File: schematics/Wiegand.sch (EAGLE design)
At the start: 66 parts, among them IC1 MC33269ST-3.3T3, J1 AVR_SPI_PRG_6NS, Q1 NTR1P02T1G, Q2 NTR1P02T1G, U1 ATMEGA168, U2 RS485_SP491, U4 MOC3063, U5 MOC3063, U6 MOC3063, U7 MOC3063, U8 MOC3063, U9 MOC3063, Y1 16Mhz

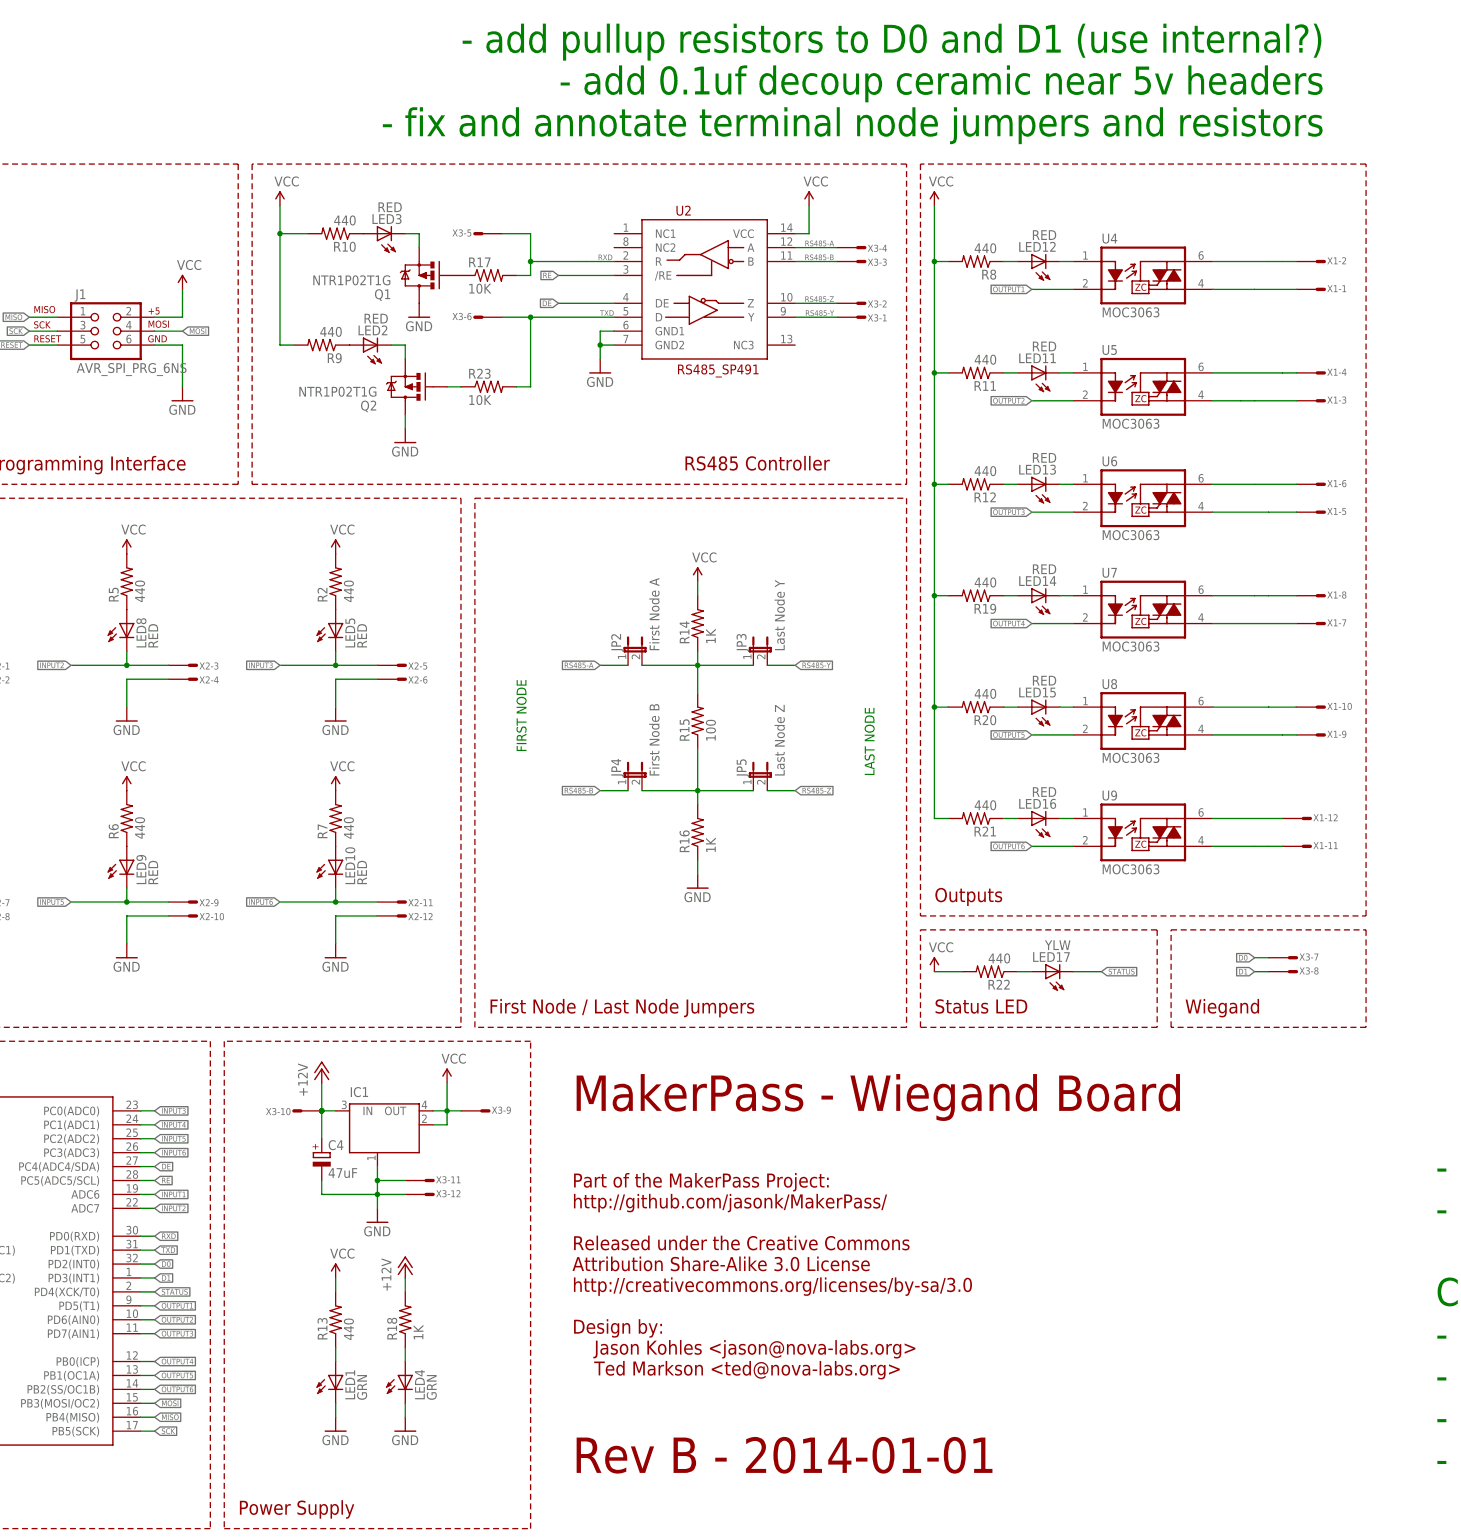
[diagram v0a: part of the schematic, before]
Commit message: added separate resistors for first / last node, added transistor option atop optoisolators
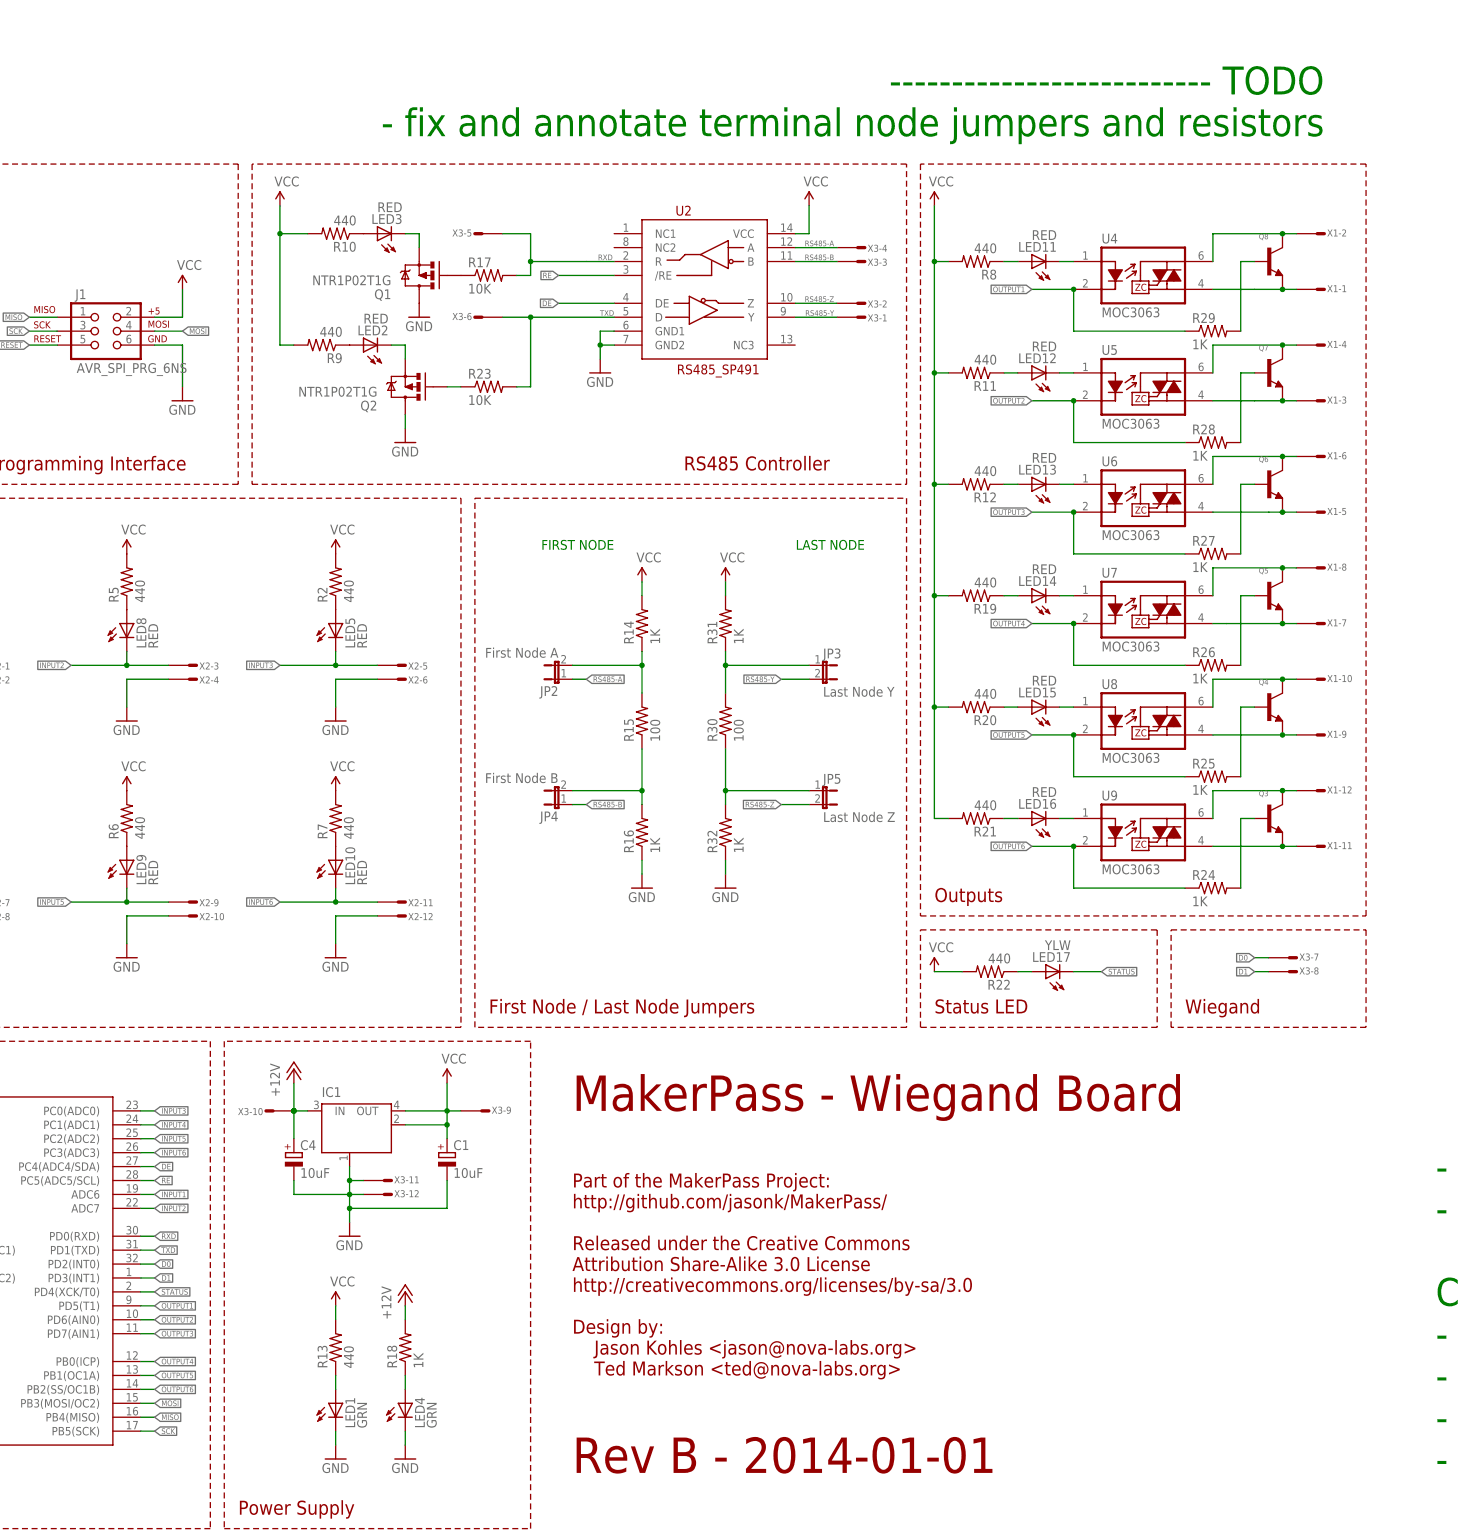
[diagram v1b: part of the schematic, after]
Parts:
- added C1: 10uF, rcl:CPOL-EUD
- added Q3, Q4, Q5, Q6, Q7, Q8: (no value), LumisenseV6:NPN-BEC-SOT23-3
- added R24, R25, R26, R27, R28, R29, R31, R32: 1K, SparkFun:RESISTOR0603-RES
- added R30: 100, SparkFun:RESISTOR0603-RES
- C4: value 47uF -> 10uF; MFG_PN EMVA250ADA470MF55G -> EMVA250ADA100MD55G
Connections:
- new net N$43: Q4.B, R25.2
- new net N$435: Q3.B, R24.2
- new net N$44: Q5.B, R26.2
- new net N$48: Q6.B, R27.2
- new net N$49: Q7.B, R28.2
- new net N$50: Q8.B, R29.2
- new net N$51: JP2.2, R14.1, R15.2
- new net N$52: JP4.2, R15.1, R16.2
- net GND: now also C1.-, R32.1
- net N$15: now also LED11.C; no longer LED12.C
- net N$16: now also LED11.A; no longer LED12.A
- net N$17: now also Q8.E
- net N$18: now also Q8.C
- net N$19: now also Q7.E
- net N$20: now also Q7.C
- net N$21: now also LED12.A; no longer LED11.A
- net N$22: now also LED12.C; no longer LED11.C
- net N$23: now also Q6.E
- net N$24: now also Q6.C
- net N$29: now also Q5.E
- net N$3: now also Q4.E
- net N$30: now also Q5.C
- net N$37: now also Q3.C, U9.T1, X1-12.S; no longer U9.T2, X1-11.S
- net N$38: now also Q3.E, U9.T2, X1-11.S; no longer U9.T1, X1-12.S
- net N$4: now also Q4.C
- net N$6: now also R30.1, R32.2; no longer JP4.2, R15.1, R16.2
- net N$7: now also R30.2, R31.1; no longer JP2.2, R14.1, R15.2
- net OUTPUT1: now also R29.1
- net OUTPUT2: now also R28.1
- net OUTPUT3: now also R27.1
- net OUTPUT4: now also R26.1
- net OUTPUT5: now also R25.1
- net OUTPUT6: now also R24.1
- net VCC: now also C1.+, R31.2
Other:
- note added: "-------------------------- TODO - fix and annotate terminal node jumpers and resistors"
- note removed: "- add pullup resistors to D0 and D1 (use internal?) - add 0.1uf decoup ceramic near 5v headers - fix and annotate terminal node jumpers and resistors"
- moved on the sheet: C4, IC1, JP2, JP3, JP4, JP5, LED1, LED11, LED12, LED4, R13, R14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
